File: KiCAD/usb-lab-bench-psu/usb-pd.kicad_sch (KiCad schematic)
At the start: 26 parts, among them J2 USB_PD_Receptacle, J3 Conn_02x03_Top_Bottom, Q1 PMOS, Q2 PMOS, U1 STUSB4500QTR

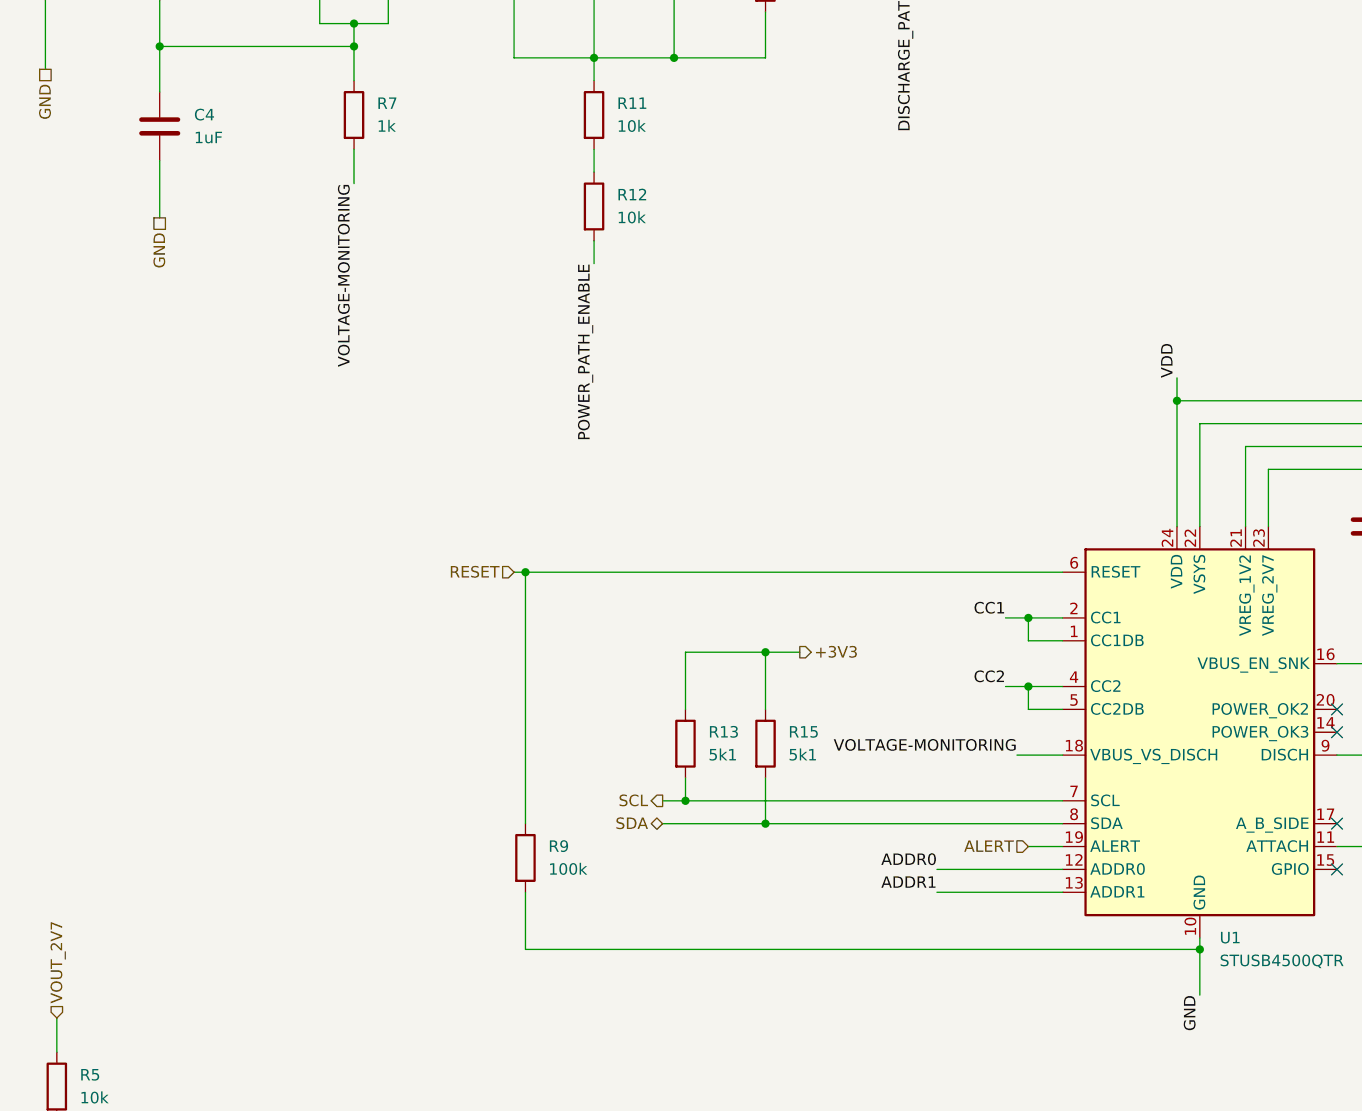
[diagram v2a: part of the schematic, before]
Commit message: restructured schematics to better show individual boards
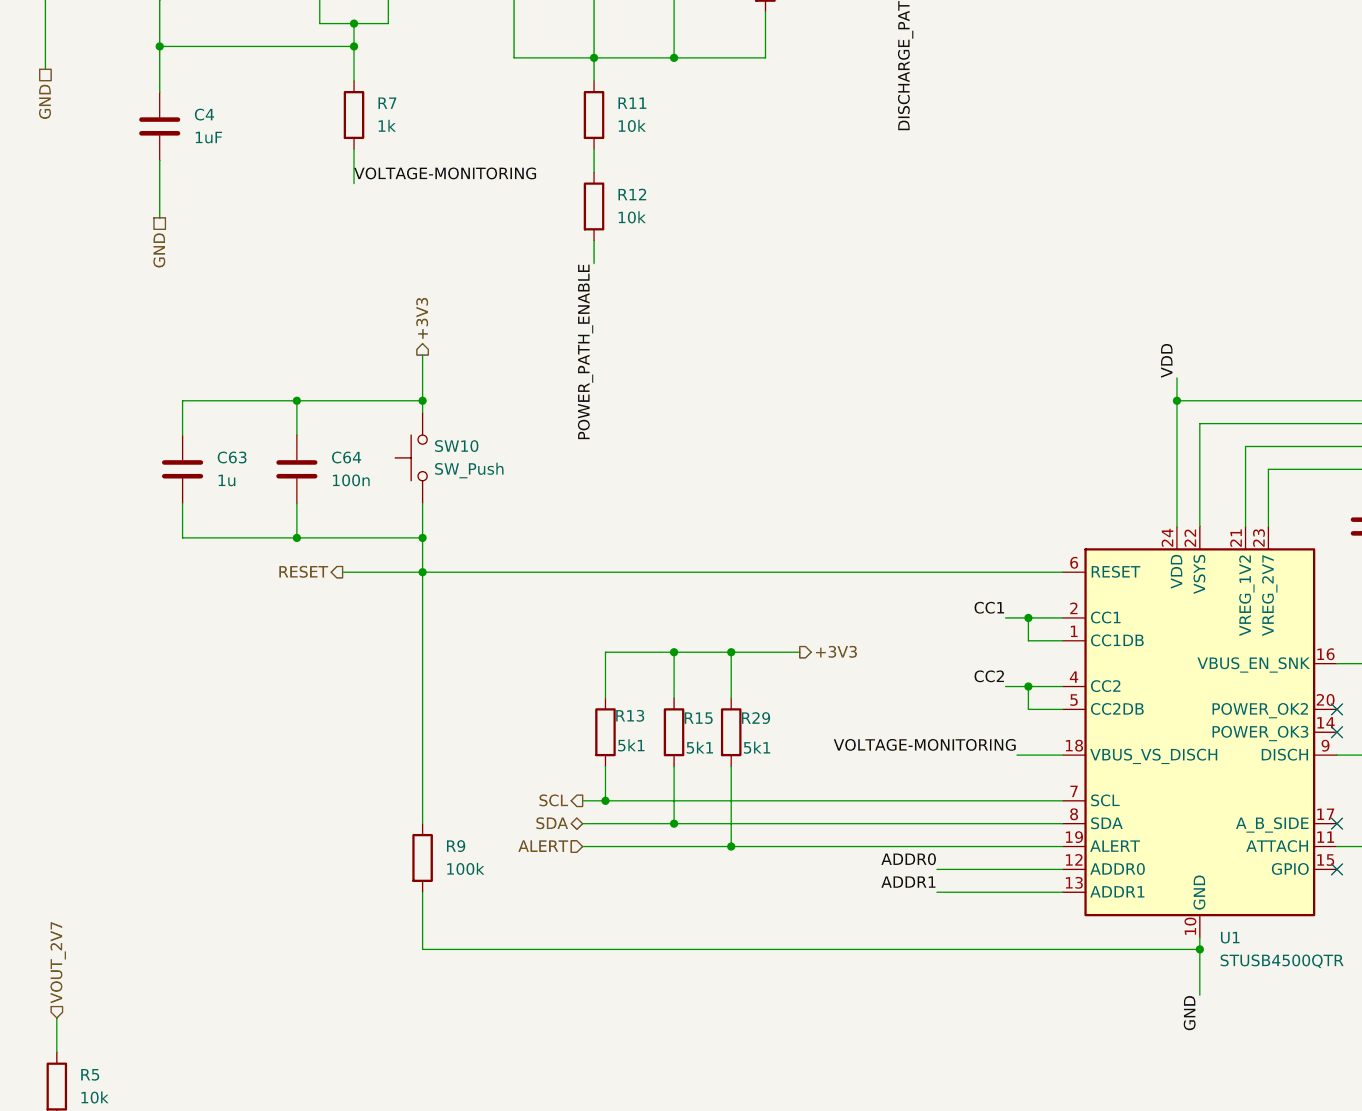
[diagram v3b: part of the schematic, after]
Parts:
- added C63: 1u, Capacitor_SMD:C_0402_1005Metric_Pad0.74x0.62mm_HandSolder, symbol Device:C
- added C64: 100n, Capacitor_SMD:C_0402_1005Metric_Pad0.74x0.62mm_HandSolder, symbol Device:C
- added R29: 5k1, symbol Device:R
- added SW10: SW_Push, Button_Switch_SMD:SW_SPST_TL3342, symbol Switch:SW_Push
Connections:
- net +3V3: now also C63.1, C64.1, R29.1, SW10.2
- net ALERT: now also R29.2
- net RESET: now also C63.2, C64.2, SW10.1
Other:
- moved on the sheet: R13, R15, R9

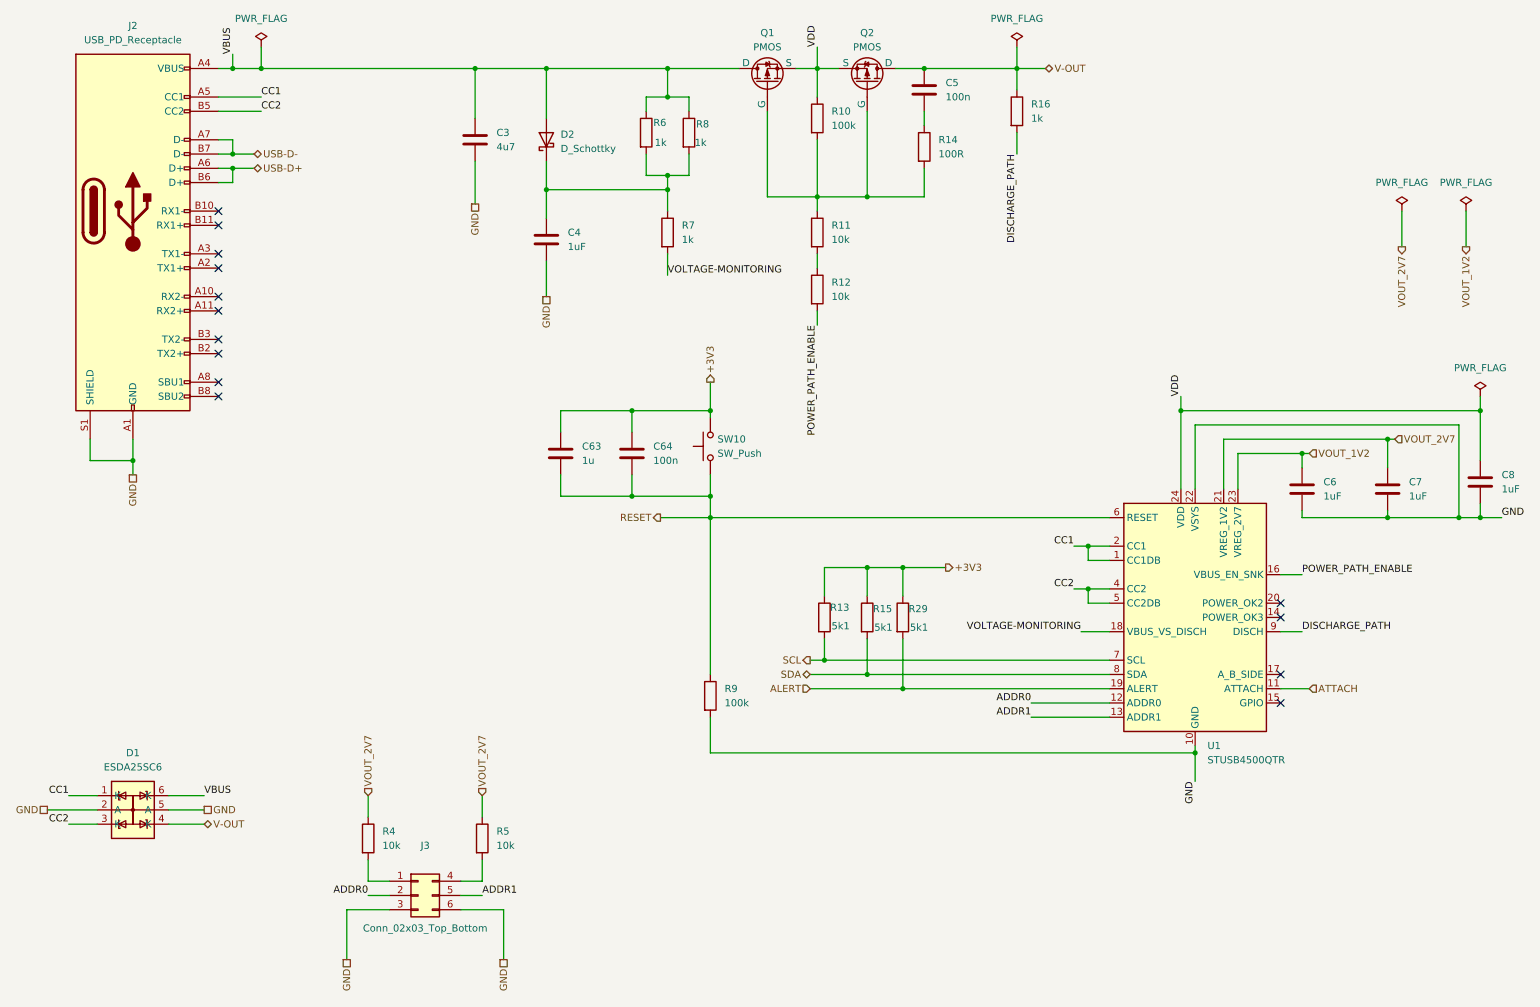
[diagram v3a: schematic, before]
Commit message: added current limiting circuit for USB PD sink, added 2nd buck converter
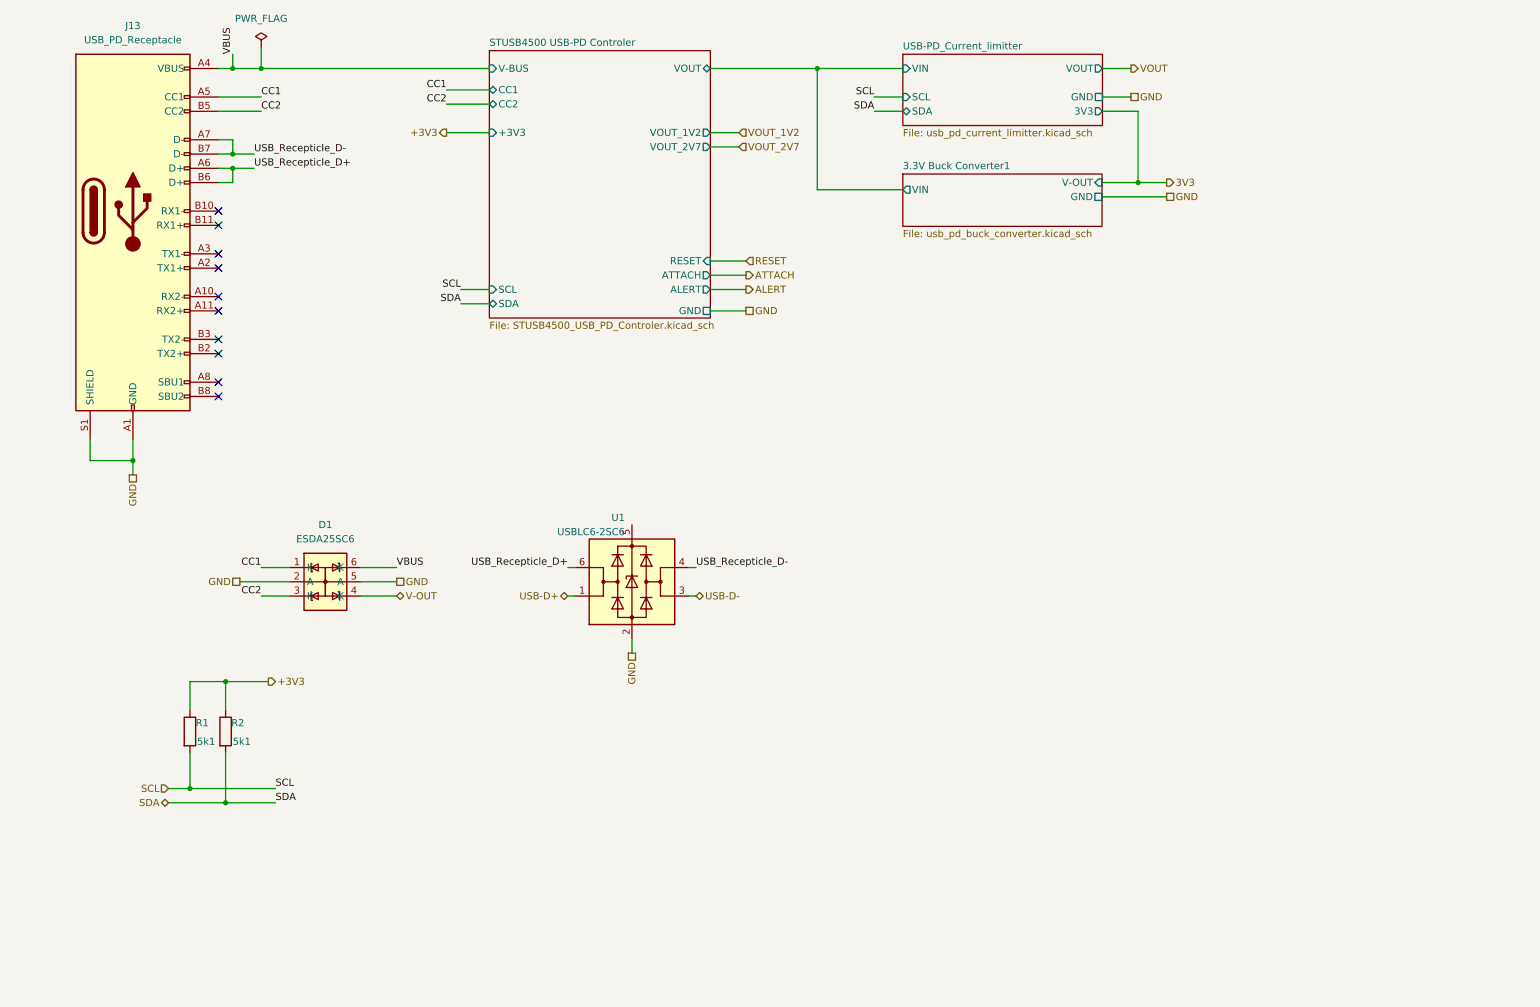
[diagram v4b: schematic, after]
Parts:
- removed C3: 4u7, symbol Device:C
- removed C4, C6, C7, C8: 1uF, symbol Device:C
- removed C5: 100n, symbol Device:C
- removed C63: 1u, Capacitor_SMD:C_0402_1005Metric_Pad0.74x0.62mm_HandSolder, symbol Device:C
- removed C64: 100n, Capacitor_SMD:C_0402_1005Metric_Pad0.74x0.62mm_HandSolder, symbol Device:C
- removed D2: D_Schottky, symbol Device:D_Schottky
- removed J3: Conn_02x03_Top_Bottom, symbol Connector_Generic:Conn_02x03_Top_Bottom
- removed Q1, Q2: PMOS, symbol Simulation_SPICE:PMOS
- removed R10, R9: 100k, symbol Device:R
- removed R11, R12, R4, R5: 10k, symbol Device:R
- removed R13: 5k1, symbol Device:R
- removed R14: 100R, symbol Device:R
- removed R16, R6, R7, R8: 1k, symbol Device:R
- removed SW10: SW_Push, Button_Switch_SMD:SW_SPST_TL3342, symbol Switch:SW_Push
- removed U1: STUSB4500QTR, Package_DFN_QFN:QFN-24-1EP_4x4mm_P0.5mm_EP2.7x2.7mm, symbol Interface_USB:STUSB4500QTR
- added U1: USBLC6-2SC6, Package_TO_SOT_SMD:SOT-23-6, symbol Power_Protection:USBLC6-2SC6
- renumbered J2 to J13, R15 to R1, R29 to R2
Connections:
- net ALERT: no longer R2.2
- net GND: now also U1.2 (GND)
- net SCL: now also R1.2
- net SDA: now also R2.2; no longer R1.2
- net USB-D+: now also U1.1 (I/O1); no longer J13.A6 (D+), J13.B6 (D+)
- net USB-D-: now also U1.3 (I/O2); no longer J13.A7 (D-), J13.B7 (D-)
- new net USB_Recepticle_D+: J13.A6 (D+), J13.B6 (D+), U1.6 (I/O1)
- new net USB_Recepticle_D-: J13.A7 (D-), J13.B7 (D-), U1.4 (I/O2)
- no-connect marks 14 -> 10
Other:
- added sheet 3.3V Buck Converter1 (usb_pd_buck_converter.kicad_sch)
- added sheet STUSB4500 USB-PD Controler (STUSB4500_USB_PD_Controler.kicad_sch)
- added sheet USB-PD_Current_limitter (usb_pd_current_limitter.kicad_sch)
- moved on the sheet: D1, R1, R2

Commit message: Fixed label directions
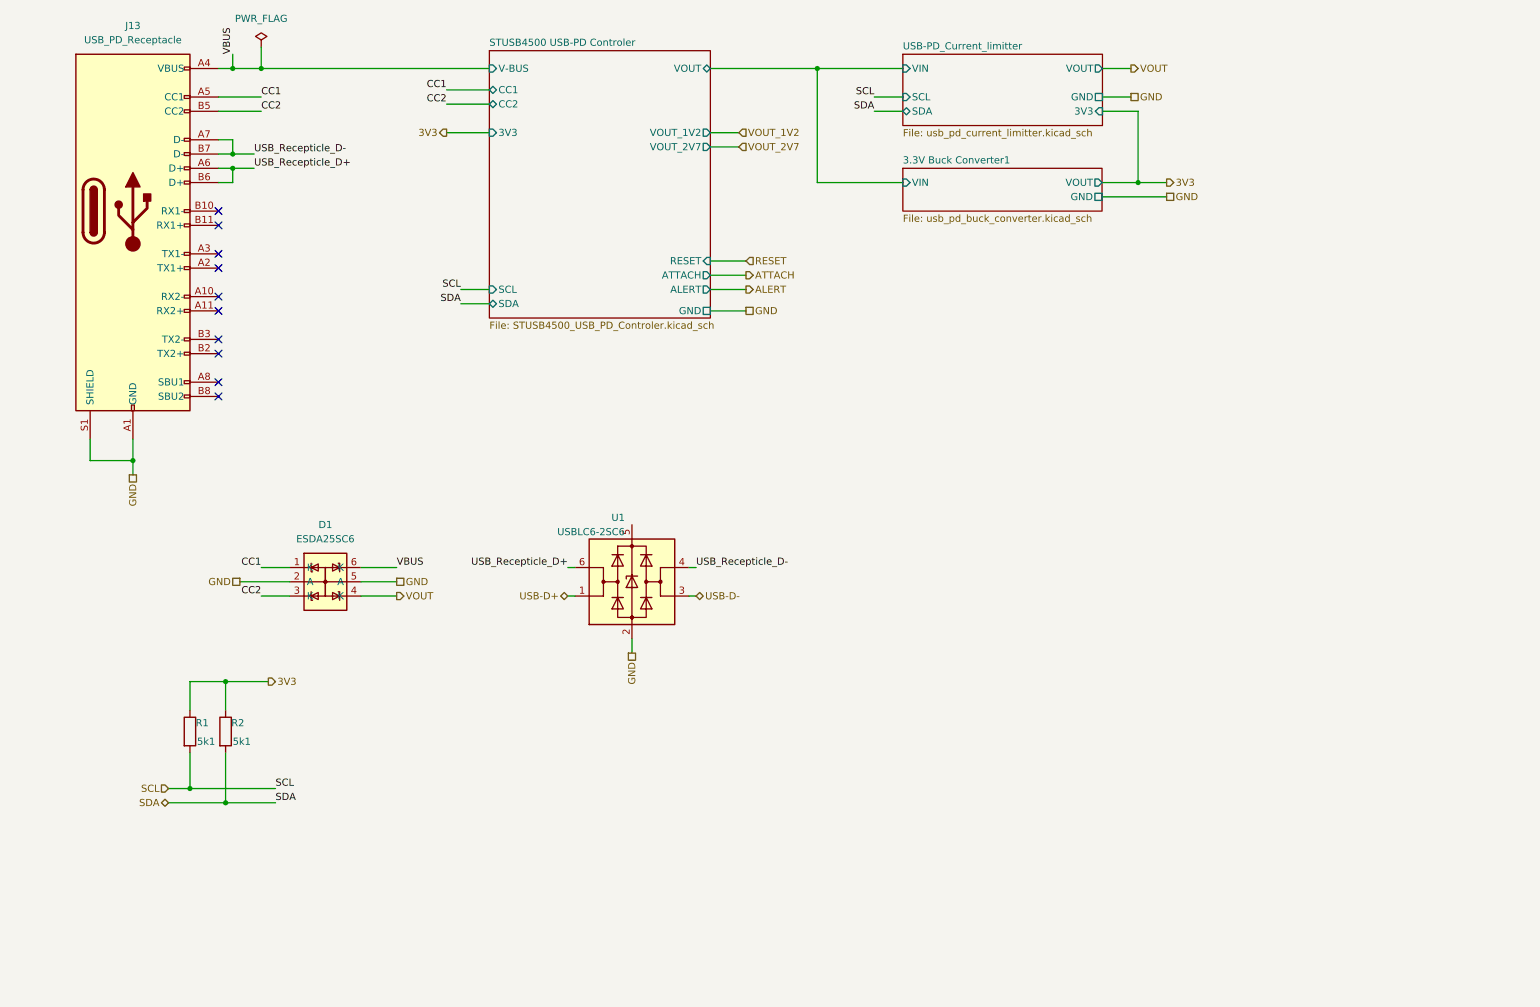
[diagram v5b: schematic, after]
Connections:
- net +3V3 is gone; now on net 3V3: R1.1, R2.1
- net V-OUT is gone; now on net VOUT: D1.4 (K)
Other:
- sheet 3.3V Buck Converter1 ports: added VOUT; removed V-OUT
- sheet STUSB4500 USB-PD Controler ports: added 3V3; removed +3V3
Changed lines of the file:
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@@
 	(wire
 		(pts
-			(xy 158.75 27.94) (xy 158.75 49.53)
+			(xy 158.75 27.94) (xy 158.75 48.26)
 		)
 		(stroke
@@
 	(wire
 		(pts
-			(xy 158.75 49.53) (xy 173.99 49.53)
+			(xy 158.75 48.26) (xy 173.99 48.26)
 		)
 		(stroke
@@
 		)
 	)
-	(hierarchical_label "V-OUT"
-		(shape bidirectional)
+	(hierarchical_label "VOUT"
+		(shape output)
 		(at 83.82 121.92 0)
 		(effects
@@
 		)
 	)
-	(hierarchical_label "+3V3"
+	(hierarchical_label "3V3"
 		(shape output)
 		(at 92.71 39.37 180)
@@
 		)
 	)
-	(hierarchical_label "+3V3"
+	(hierarchical_label "3V3"
 		(shape output)
 		(at 60.96 137.16 0)
@@
 			)
 		)
-		(pin "3V3" output
+		(pin "3V3" input
 			(at 209.55 35.56 0)
 			(effects
@@
 	)
 	(sheet
-		(at 173.99 46.736)
-		(size 35.4838 9.3218)
+		(at 173.99 45.72)
+		(size 35.4838 7.62)
 		(exclude_from_sim no)
 		(in_bom yes)
@@
 		)
 		(property "Sheetname" "3.3V Buck Converter1"
-			(at 173.99 46.0244 0)
+			(at 173.99 45.0084 0)
 			(effects
 				(font
@@
 		)
 		(property "Sheetfile" "usb_pd_buck_converter.kicad_sch"
-			(at 173.99 56.6424 0)
+			(at 173.99 53.9246 0)
 			(effects
 				(font
@@
 			)
 		)
-		(pin "V-OUT" input
+		(pin "VOUT" output
 			(at 209.4738 48.26 0)
 			(effects
@@
 			)
 		)
-		(pin "VIN" output
-			(at 173.99 49.53 180)
+		(pin "VIN" input
+			(at 173.99 48.26 180)
 			(effects
 				(font
@@
 			)
 		)
-		(pin "+3V3" input
+		(pin "3V3" input
 			(at 100.33 39.37 180)
 			(effects
